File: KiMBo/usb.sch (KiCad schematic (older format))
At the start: 19 parts, among them U1 OSD3358, U10 TPD4S012, U7 TPS2051B, U8 TPD4S012, U9 74LVC2G241

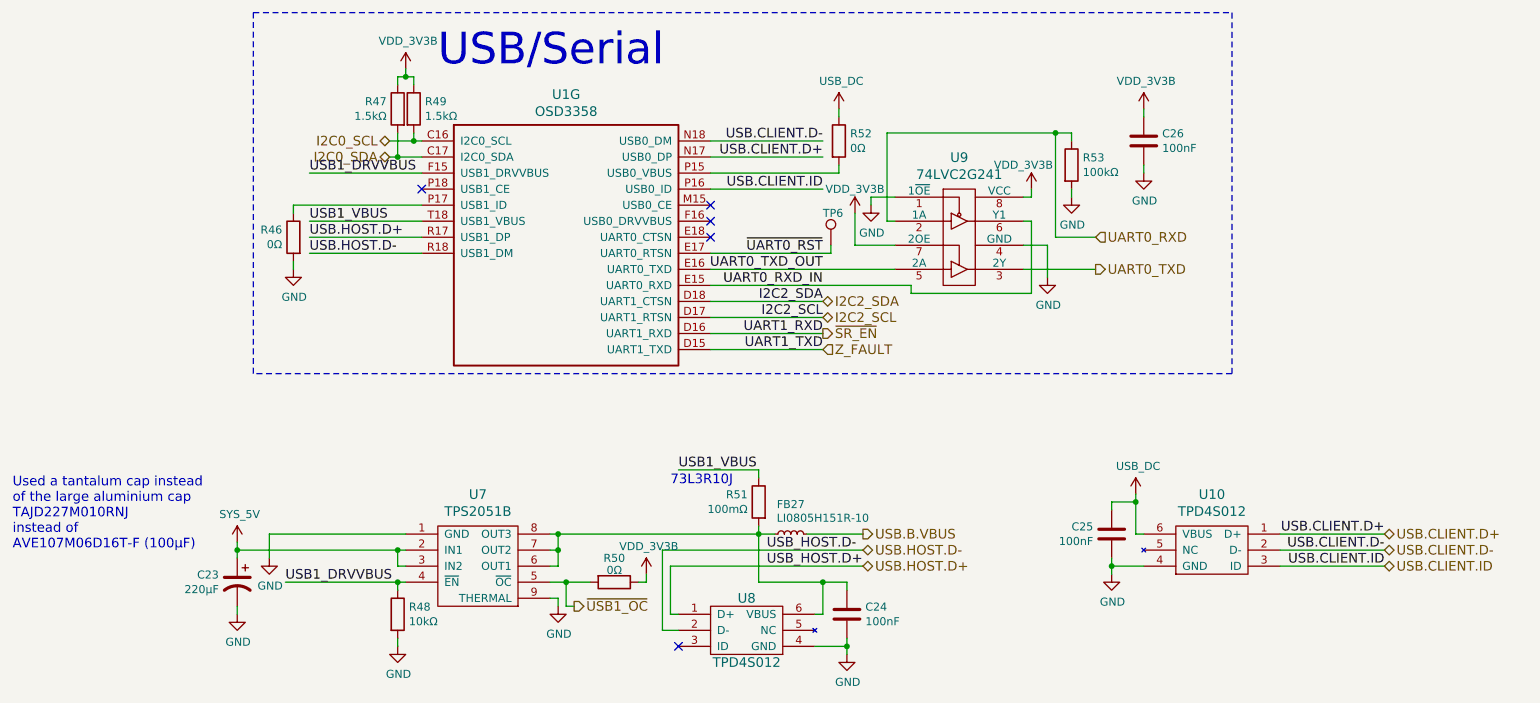
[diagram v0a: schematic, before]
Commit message: Begin layout
Arrange all connectors to get a feel for the area.
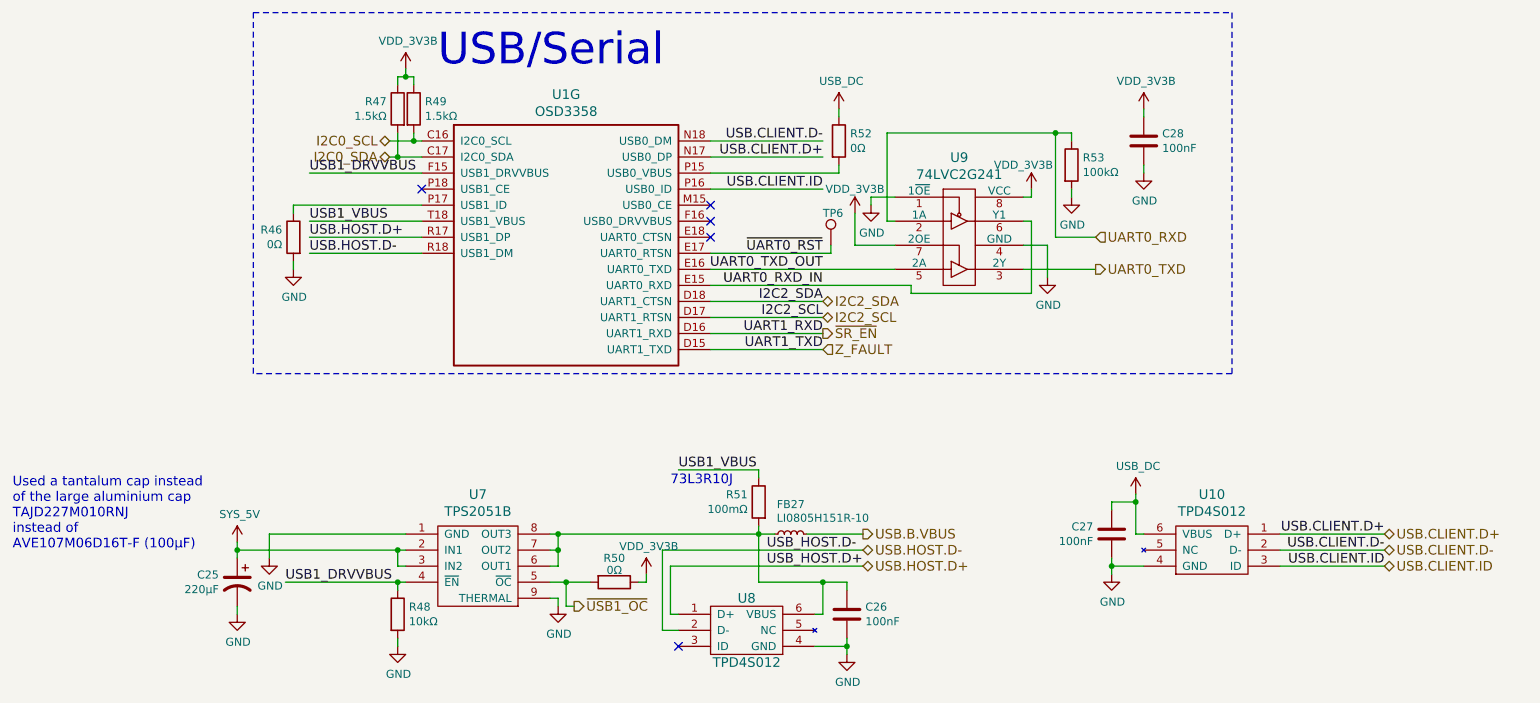
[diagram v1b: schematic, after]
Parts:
- renumbered C23 to C25, C24 to C26, C25 to C27, C26 to C28
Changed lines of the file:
@@
 $EndComp
 $Comp
-L GND #PWR0102
+L GND #PWR0105
 U 1 1 584F5078
 P 7550 2500
-F 0 "#PWR0102" H 7550 2250 50  0001 C CNN
+F 0 "#PWR0105" H 7550 2250 50  0001 C CNN
 F 1 "GND" H 7555 2327 50  0000 C CNN
 F 2 "" H 7550 2500 50  0000 C CNN
@@
 $EndComp
 $Comp
-L GND #PWR0103
+L GND #PWR0106
 U 1 1 584F508C
 P 6450 2050
-F 0 "#PWR0103" H 6450 1800 50  0001 C CNN
+F 0 "#PWR0106" H 6450 1800 50  0001 C CNN
 F 1 "GND" H 6455 1877 50  0000 C CNN
 F 2 "" H 6450 2050 50  0000 C CNN
@@
 UART0_TXD_OUT
 $Comp
-L GND #PWR0104
+L GND #PWR0107
 U 1 1 584F509A
 P 7700 2000
-F 0 "#PWR0104" H 7700 1750 50  0001 C CNN
+F 0 "#PWR0107" H 7700 1750 50  0001 C CNN
 F 1 "GND" H 7705 1827 50  0000 C CNN
 F 2 "" H 7700 2000 50  0000 C CNN
@@
 $EndComp
 $Comp
-L C C26
+L C C28
 U 1 1 584F50A3
 P 8150 1650
-F 0 "C26" H 8265 1696 50  0000 L CNN
+F 0 "C28" H 8265 1696 50  0000 L CNN
 F 1 "100nF" H 8265 1605 50  0000 L CNN
 F 2 "Capacitors_SMD:C_0603" H 8150 1650 50  0001 C CNN
@@
 $EndComp
 $Comp
-L GND #PWR0105
+L GND #PWR0108
 U 1 1 584F50AA
 P 8150 1850
-F 0 "#PWR0105" H 8150 1600 50  0001 C CNN
+F 0 "#PWR0108" H 8150 1600 50  0001 C CNN
 F 1 "GND" H 8155 1677 50  0000 C CNN
 F 2 "" H 8150 1850 50  0000 C CNN
@@
 $EndComp
 $Comp
-L GND #PWR0106
+L GND #PWR0109
 U 1 1 584F50D8
 P 2850 2450
-F 0 "#PWR0106" H 2850 2200 50  0001 C CNN
+F 0 "#PWR0109" H 2850 2200 50  0001 C CNN
 F 1 "GND" H 2855 2277 50  0000 C CNN
 F 2 "" H 2850 2450 50  0000 C CNN
@@
 $EndComp
 $Comp
-L C C24
+L C C26
 U 1 1 58524285
 P 6300 4600
-F 0 "C24" H 6415 4646 50  0000 L CNN
+F 0 "C26" H 6415 4646 50  0000 L CNN
 F 1 "100nF" H 6415 4555 50  0000 L CNN
 F 2 "Capacitors_SMD:C_0603" H 6300 4600 50  0001 C CNN
@@
 $EndComp
 $Comp
-L GND #PWR0107
+L GND #PWR0110
 U 1 1 585243B8
 P 6300 4850
-F 0 "#PWR0107" H 6300 4600 50  0001 C CNN
+F 0 "#PWR0110" H 6300 4600 50  0001 C CNN
 F 1 "GND" H 6305 4677 50  0000 C CNN
 F 2 "" H 6300 4850 50  0000 C CNN
@@
 $EndComp
 $Comp
-L GND #PWR0108
+L GND #PWR0111
 U 1 1 58528602
 P 4500 4550
-F 0 "#PWR0108" H 4500 4300 50  0001 C CNN
+F 0 "#PWR0111" H 4500 4300 50  0001 C CNN
 F 1 "GND" H 4505 4377 50  0000 C CNN
 F 2 "" H 4500 4550 50  0000 C CNN
@@
 $EndComp
 $Comp
-L GND #PWR0109
+L GND #PWR0112
 U 1 1 5852A6BE
 P 2500 4600
-F 0 "#PWR0109" H 2500 4350 50  0001 C CNN
+F 0 "#PWR0112" H 2500 4350 50  0001 C CNN
 F 1 "GND" H 2505 4427 50  0000 C CNN
 F 2 "" H 2500 4600 50  0000 C CNN
@@
 $EndComp
 $Comp
-L GND #PWR0110
+L GND #PWR0113
 U 1 1 5852A82F
 P 2700 4250
-F 0 "#PWR0110" H 2700 4000 50  0001 C CNN
+F 0 "#PWR0113" H 2700 4000 50  0001 C CNN
 F 1 "GND" H 2705 4077 50  0000 C CNN
 F 2 "" H 2700 4250 50  0000 C CNN
@@
 $EndComp
 $Comp
-L GND #PWR0111
+L GND #PWR0114
 U 1 1 5852B68C
 P 3500 4800
-F 0 "#PWR0111" H 3500 4550 50  0001 C CNN
+F 0 "#PWR0114" H 3500 4550 50  0001 C CNN
 F 1 "GND" H 3505 4627 50  0000 C CNN
 F 2 "" H 3500 4800 50  0000 C CNN
@@
 $EndComp
 $Comp
-L C C25
+L C C27
 U 1 1 5852C2E6
 P 7950 4100
-F 0 "C25" H 8065 4146 50  0000 L CNN
+F 0 "C27" H 8065 4146 50  0000 L CNN
 F 1 "100nF" H 8065 4055 50  0000 L CNN
 F 2 "Capacitors_SMD:C_0603" H 7950 4100 50  0001 C CNN
@@
 I2C2_SDA
 $Comp
-L USB_DC #PWR0112
+L USB_DC #PWR0115
 U 1 1 59F94F9A
 P 8100 3850
-F 0 "#PWR0112" H 8100 3700 50  0001 C CNN
+F 0 "#PWR0115" H 8100 3700 50  0001 C CNN
 F 1 "USB_DC" H 8115 4023 50  0000 C CNN
 F 2 "" H 8100 3850 50  0000 C CNN
@@
 $EndComp
 $Comp
-L SYS_5V #PWR0113
+L SYS_5V #PWR0116
 U 1 1 59F970D0
 P 2500 4150
-F 0 "#PWR0113" H 2500 4000 50  0001 C CNN
+F 0 "#PWR0116" H 2500 4000 50  0001 C CNN
 F 1 "SYS_5V" H 2515 4323 50  0000 C CNN
 F 2 "" H 2500 4150 50  0000 C CNN
@@
 $EndComp
 $Comp
-L VDD_3V3B #PWR0114
+L VDD_3V3B #PWR0117
 U 1 1 59FBF8B1
 P 6350 2100
-F 0 "#PWR0114" H 6350 1950 50  0001 C CNN
+F 0 "#PWR0117" H 6350 1950 50  0001 C CNN
 F 1 "VDD_3V3B" H 6350 2250 50  0000 C CNN
 F 2 "" H 6350 2100 50  0000 C CNN
@@
 $EndComp
 $Comp
-L VDD_3V3B #PWR0115
+L VDD_3V3B #PWR0118
 U 1 1 59FBF8FC
 P 7450 1950
-F 0 "#PWR0115" H 7450 1800 50  0001 C CNN
+F 0 "#PWR0118" H 7450 1800 50  0001 C CNN
 F 1 "VDD_3V3B" H 7400 2100 50  0000 C CNN
 F 2 "" H 7450 1950 50  0000 C CNN
@@
 $EndComp
 $Comp
-L VDD_3V3B #PWR0116
+L VDD_3V3B #PWR0119
 U 1 1 59FC0162
 P 8150 1450
-F 0 "#PWR0116" H 8150 1300 50  0001 C CNN
+F 0 "#PWR0119" H 8150 1300 50  0001 C CNN
 F 1 "VDD_3V3B" H 8165 1623 50  0000 C CNN
 F 2 "" H 8150 1450 50  0000 C CNN
@@
 $EndComp
 $Comp
-L USB_DC #PWR0117
+L USB_DC #PWR0120
 U 1 1 59FEDDB0
 P 6250 1450
-F 0 "#PWR0117" H 6250 1300 50  0001 C CNN
+F 0 "#PWR0120" H 6250 1300 50  0001 C CNN
 F 1 "USB_DC" H 6265 1623 50  0000 C CNN
 F 2 "" H 6250 1450 50  0000 C CNN
@@
 $EndComp
 $Comp
-L VDD_3V3B #PWR0118
+L VDD_3V3B #PWR0121
 U 1 1 5A01DA26
 P 3550 1200
-F 0 "#PWR0118" H 3550 1050 50  0001 C CNN
+F 0 "#PWR0121" H 3550 1050 50  0001 C CNN
 F 1 "VDD_3V3B" H 3565 1373 50  0000 C CNN
 F 2 "" H 3550 1200 50  0000 C CNN
@@
 Used a tantalum cap instead\nof the large aluminium cap\nTAJD227M010RNJ\ninstead of\nAVE107M06D16T-F (100μF)
 $Comp
-L VDD_3V3B #PWR0119
+L VDD_3V3B #PWR0122
 U 1 1 5AF563FC
 P 5050 4350
-F 0 "#PWR0119" H 5050 4200 50  0001 C CNN
+F 0 "#PWR0122" H 5050 4200 50  0001 C CNN
 F 1 "VDD_3V3B" H 5065 4523 50  0000 C CNN
 F 2 "" H 5050 4350 50  0000 C CNN
@@
 $EndComp
 $Comp
-L GND #PWR0120
+L GND #PWR0123
 U 1 1 5BC77EEA
 P 7950 4350
-F 0 "#PWR0120" H 7950 4100 50  0001 C CNN
+F 0 "#PWR0123" H 7950 4100 50  0001 C CNN
 F 1 "GND" H 7955 4177 50  0000 C CNN
 F 2 "" H 7950 4350 50  0000 C CNN
@@
 73L3R10J
 $Comp
-L CP1 C23
+L CP1 C25
 U 1 1 58EB0DF2
 P 2500 4400
-F 0 "C23" H 2615 4446 50  0000 L CNN
+F 0 "C25" H 2615 4446 50  0000 L CNN
 F 1 "220μF" H 2615 4355 50  0000 L CNN
 F 2 "Capacitors_Tantalum_SMD:TantalC_SizeD_EIA-7343_Reflow" H 2500 4400 50  0001 C CNN

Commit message: Remove HDMI from the schematic
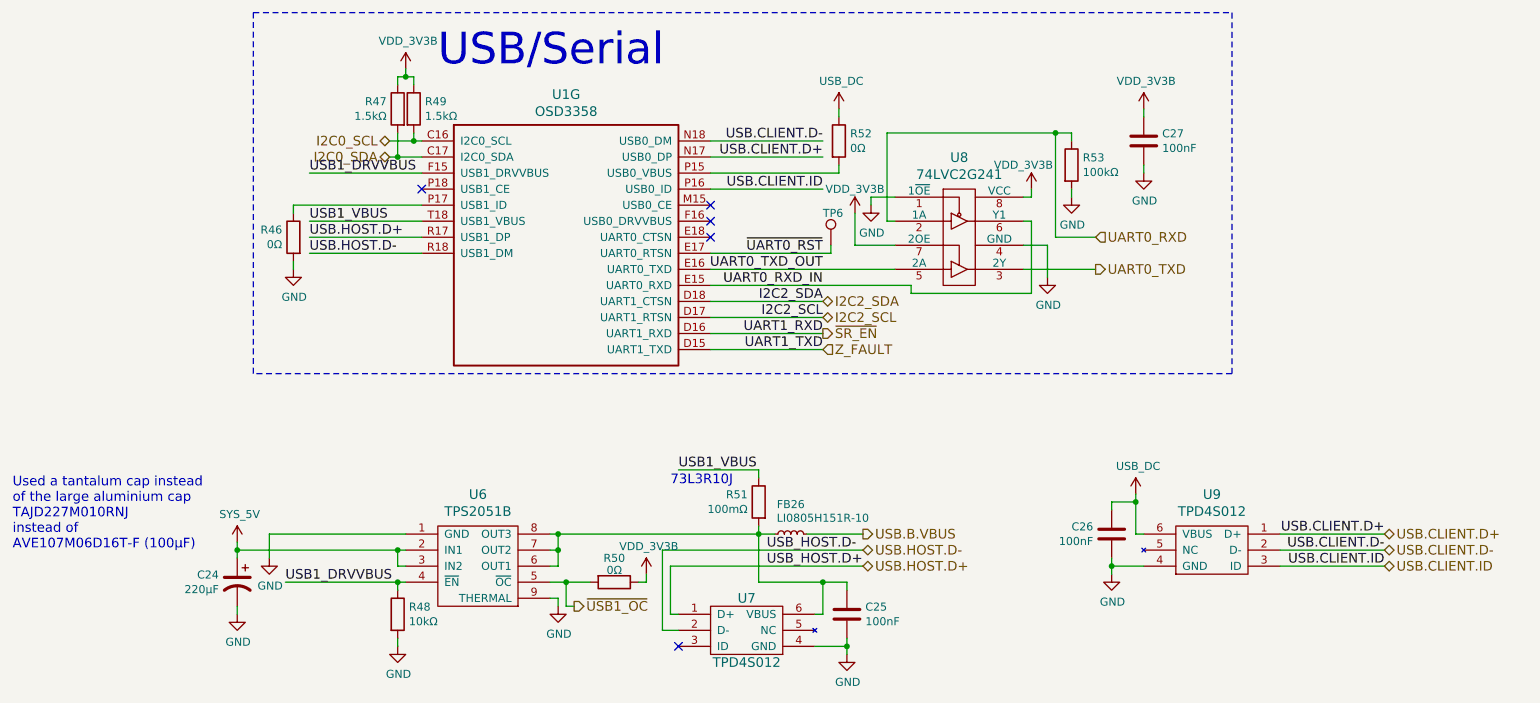
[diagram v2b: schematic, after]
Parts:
- renumbered C25 to C24, C26 to C25, C27 to C26, C28 to C27, FB27 to FB26, U7 to U6, U8 to U7, U9 to U8, U10 to U9
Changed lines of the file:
@@
 $Descr A4 11693 8268
 encoding utf-8
-Sheet 7 26
+Sheet 7 25
 Title ""
 Date ""
@@
 $EndComp
 $Comp
-L 74LVC2G241 U9
+L 74LVC2G241 U8
 U 1 1 584F506B
 P 7000 2200
-F 0 "U9" H 7000 2647 60  0000 C CNN
+F 0 "U8" H 7000 2647 60  0000 C CNN
 F 1 "74LVC2G241" H 7000 2541 60  0000 C CNN
 F 2 "KiMBo:DCT-MSOP-8_3x3mm_Pitch0.65mm" H 7050 1950 60  0001 C CNN
@@
 $EndComp
 $Comp
-L GND #PWR0105
+L GND #PWR0100
 U 1 1 584F5078
 P 7550 2500
-F 0 "#PWR0105" H 7550 2250 50  0001 C CNN
+F 0 "#PWR0100" H 7550 2250 50  0001 C CNN
 F 1 "GND" H 7555 2327 50  0000 C CNN
 F 2 "" H 7550 2500 50  0000 C CNN
@@
 $EndComp
 $Comp
-L GND #PWR0106
+L GND #PWR0101
 U 1 1 584F508C
 P 6450 2050
-F 0 "#PWR0106" H 6450 1800 50  0001 C CNN
+F 0 "#PWR0101" H 6450 1800 50  0001 C CNN
 F 1 "GND" H 6455 1877 50  0000 C CNN
 F 2 "" H 6450 2050 50  0000 C CNN
@@
 UART0_TXD_OUT
 $Comp
-L GND #PWR0107
+L GND #PWR0102
 U 1 1 584F509A
 P 7700 2000
-F 0 "#PWR0107" H 7700 1750 50  0001 C CNN
+F 0 "#PWR0102" H 7700 1750 50  0001 C CNN
 F 1 "GND" H 7705 1827 50  0000 C CNN
 F 2 "" H 7700 2000 50  0000 C CNN
@@
 $EndComp
 $Comp
-L C C28
+L C C27
 U 1 1 584F50A3
 P 8150 1650
-F 0 "C28" H 8265 1696 50  0000 L CNN
+F 0 "C27" H 8265 1696 50  0000 L CNN
 F 1 "100nF" H 8265 1605 50  0000 L CNN
 F 2 "Capacitors_SMD:C_0603" H 8150 1650 50  0001 C CNN
@@
 $EndComp
 $Comp
-L GND #PWR0108
+L GND #PWR0103
 U 1 1 584F50AA
 P 8150 1850
-F 0 "#PWR0108" H 8150 1600 50  0001 C CNN
+F 0 "#PWR0103" H 8150 1600 50  0001 C CNN
 F 1 "GND" H 8155 1677 50  0000 C CNN
 F 2 "" H 8150 1850 50  0000 C CNN
@@
 $EndComp
 $Comp
-L GND #PWR0109
+L GND #PWR0104
 U 1 1 584F50D8
 P 2850 2450
-F 0 "#PWR0109" H 2850 2200 50  0001 C CNN
+F 0 "#PWR0104" H 2850 2200 50  0001 C CNN
 F 1 "GND" H 2855 2277 50  0000 C CNN
 F 2 "" H 2850 2450 50  0000 C CNN
@@
 USB_HOST.D+
 $Comp
-L TPD4S012 U8
+L TPD4S012 U7
 U 1 1 58523D44
 P 5650 4700
-F 0 "U8" H 5675 4900 60  0000 C CNN
+F 0 "U7" H 5675 4900 60  0000 C CNN
 F 1 "TPD4S012" H 5675 4500 60  0000 C CNN
 F 2 "KiMBo:DRY-DFN-6-1EP_2x2mm_Pitch0.5mm" H 5650 4700 60  0001 C CNN
@@
 $EndComp
 $Comp
-L C C26
+L C C25
 U 1 1 58524285
 P 6300 4600
-F 0 "C26" H 6415 4646 50  0000 L CNN
+F 0 "C25" H 6415 4646 50  0000 L CNN
 F 1 "100nF" H 6415 4555 50  0000 L CNN
 F 2 "Capacitors_SMD:C_0603" H 6300 4600 50  0001 C CNN
@@
 $EndComp
 $Comp
-L GND #PWR0110
+L GND #PWR0105
 U 1 1 585243B8
 P 6300 4850
-F 0 "#PWR0110" H 6300 4600 50  0001 C CNN
+F 0 "#PWR0105" H 6300 4600 50  0001 C CNN
 F 1 "GND" H 6305 4677 50  0000 C CNN
 F 2 "" H 6300 4850 50  0000 C CNN
@@
 USB1_VBUS
 $Comp
-L TPS2051B U7
+L TPS2051B U6
 U 1 1 58527077
 P 4000 4250
-F 0 "U7" H 4000 4647 60  0000 C CNN
+F 0 "U6" H 4000 4647 60  0000 C CNN
 F 1 "TPS2051B" H 4000 4541 60  0000 C CNN
 F 2 "KiMBo:DGN-MSOP-8_3x3mm_Pitch0.65mm" H 4000 4200 60  0001 C CNN
@@
 $EndComp
 $Comp
-L GND #PWR0111
+L GND #PWR0106
 U 1 1 58528602
 P 4500 4550
-F 0 "#PWR0111" H 4500 4300 50  0001 C CNN
+F 0 "#PWR0106" H 4500 4300 50  0001 C CNN
 F 1 "GND" H 4505 4377 50  0000 C CNN
 F 2 "" H 4500 4550 50  0000 C CNN
@@
 $EndComp
 $Comp
-L GND #PWR0112
+L GND #PWR0107
 U 1 1 5852A6BE
 P 2500 4600
-F 0 "#PWR0112" H 2500 4350 50  0001 C CNN
+F 0 "#PWR0107" H 2500 4350 50  0001 C CNN
 F 1 "GND" H 2505 4427 50  0000 C CNN
 F 2 "" H 2500 4600 50  0000 C CNN
@@
 $EndComp
 $Comp
-L GND #PWR0113
+L GND #PWR0108
 U 1 1 5852A82F
 P 2700 4250
-F 0 "#PWR0113" H 2700 4000 50  0001 C CNN
+F 0 "#PWR0108" H 2700 4000 50  0001 C CNN
 F 1 "GND" H 2705 4077 50  0000 C CNN
 F 2 "" H 2700 4250 50  0000 C CNN
@@
 $EndComp
 $Comp
-L GND #PWR0114
+L GND #PWR0109
 U 1 1 5852B68C
 P 3500 4800
-F 0 "#PWR0114" H 3500 4550 50  0001 C CNN
+F 0 "#PWR0109" H 3500 4550 50  0001 C CNN
 F 1 "GND" H 3505 4627 50  0000 C CNN
 F 2 "" H 3500 4800 50  0000 C CNN
@@
 $EndComp
 $Comp
-L TPD4S012 U10
+L TPD4S012 U9
 U 1 1 5852BD3E
 P 8600 4200
-F 0 "U10" H 8625 4547 60  0000 C CNN
+F 0 "U9" H 8625 4547 60  0000 C CNN
 F 1 "TPD4S012" H 8625 4441 60  0000 C CNN
 F 2 "KiMBo:DRY-DFN-6-1EP_2x2mm_Pitch0.5mm" H 8600 4200 60  0001 C CNN
@@
 $EndComp
 $Comp
-L C C27
+L C C26
 U 1 1 5852C2E6
 P 7950 4100
-F 0 "C27" H 8065 4146 50  0000 L CNN
+F 0 "C26" H 8065 4146 50  0000 L CNN
 F 1 "100nF" H 8065 4055 50  0000 L CNN
 F 2 "Capacitors_SMD:C_0603" H 7950 4100 50  0001 C CNN
@@
 USB.CLIENT.ID
 $Comp
-L INDUCTOR_Small FB27
+L INDUCTOR_Small FB26
 U 1 1 58E84972
 P 5950 4100
-F 0 "FB27" V 6135 4100 50  0000 C CNN
+F 0 "FB26" V 6135 4100 50  0000 C CNN
 F 1 "LI0805H151R-10" V 6050 3900 50  0000 C CNN
 F 2 "Resistors_SMD:R_0805" H 5950 4100 50  0001 C CNN
@@
 I2C2_SDA
 $Comp
-L USB_DC #PWR0115
+L USB_DC #PWR0110
 U 1 1 59F94F9A
 P 8100 3850
-F 0 "#PWR0115" H 8100 3700 50  0001 C CNN
+F 0 "#PWR0110" H 8100 3700 50  0001 C CNN
 F 1 "USB_DC" H 8115 4023 50  0000 C CNN
 F 2 "" H 8100 3850 50  0000 C CNN
@@
 $EndComp
 $Comp
-L SYS_5V #PWR0116
+L SYS_5V #PWR0111
 U 1 1 59F970D0
 P 2500 4150
-F 0 "#PWR0116" H 2500 4000 50  0001 C CNN
+F 0 "#PWR0111" H 2500 4000 50  0001 C CNN
 F 1 "SYS_5V" H 2515 4323 50  0000 C CNN
 F 2 "" H 2500 4150 50  0000 C CNN
@@
 $EndComp
 $Comp
-L VDD_3V3B #PWR0117
+L VDD_3V3B #PWR0112
 U 1 1 59FBF8B1
 P 6350 2100
-F 0 "#PWR0117" H 6350 1950 50  0001 C CNN
+F 0 "#PWR0112" H 6350 1950 50  0001 C CNN
 F 1 "VDD_3V3B" H 6350 2250 50  0000 C CNN
 F 2 "" H 6350 2100 50  0000 C CNN
@@
 $EndComp
 $Comp
-L VDD_3V3B #PWR0118
+L VDD_3V3B #PWR0113
 U 1 1 59FBF8FC
 P 7450 1950
-F 0 "#PWR0118" H 7450 1800 50  0001 C CNN
+F 0 "#PWR0113" H 7450 1800 50  0001 C CNN
 F 1 "VDD_3V3B" H 7400 2100 50  0000 C CNN
 F 2 "" H 7450 1950 50  0000 C CNN
@@
 $EndComp
 $Comp
-L VDD_3V3B #PWR0119
+L VDD_3V3B #PWR0114
 U 1 1 59FC0162
 P 8150 1450
-F 0 "#PWR0119" H 8150 1300 50  0001 C CNN
+F 0 "#PWR0114" H 8150 1300 50  0001 C CNN
 F 1 "VDD_3V3B" H 8165 1623 50  0000 C CNN
 F 2 "" H 8150 1450 50  0000 C CNN
@@
 $EndComp
 $Comp
-L USB_DC #PWR0120
+L USB_DC #PWR0115
 U 1 1 59FEDDB0
 P 6250 1450
-F 0 "#PWR0120" H 6250 1300 50  0001 C CNN
+F 0 "#PWR0115" H 6250 1300 50  0001 C CNN
 F 1 "USB_DC" H 6265 1623 50  0000 C CNN
 F 2 "" H 6250 1450 50  0000 C CNN
@@
 $EndComp
 $Comp
-L VDD_3V3B #PWR0121
+L VDD_3V3B #PWR0116
 U 1 1 5A01DA26
 P 3550 1200
-F 0 "#PWR0121" H 3550 1050 50  0001 C CNN
+F 0 "#PWR0116" H 3550 1050 50  0001 C CNN
 F 1 "VDD_3V3B" H 3565 1373 50  0000 C CNN
 F 2 "" H 3550 1200 50  0000 C CNN
@@
 Used a tantalum cap instead\nof the large aluminium cap\nTAJD227M010RNJ\ninstead of\nAVE107M06D16T-F (100μF)
 $Comp
-L VDD_3V3B #PWR0122
+L VDD_3V3B #PWR0117
 U 1 1 5AF563FC
 P 5050 4350
-F 0 "#PWR0122" H 5050 4200 50  0001 C CNN
+F 0 "#PWR0117" H 5050 4200 50  0001 C CNN
 F 1 "VDD_3V3B" H 5065 4523 50  0000 C CNN
 F 2 "" H 5050 4350 50  0000 C CNN
@@
 $EndComp
 $Comp
-L GND #PWR0123
+L GND #PWR0118
 U 1 1 5BC77EEA
 P 7950 4350
-F 0 "#PWR0123" H 7950 4100 50  0001 C CNN
+F 0 "#PWR0118" H 7950 4100 50  0001 C CNN
 F 1 "GND" H 7955 4177 50  0000 C CNN
 F 2 "" H 7950 4350 50  0000 C CNN
@@
 73L3R10J
 $Comp
-L CP1 C25
+L CP1 C24
 U 1 1 58EB0DF2
 P 2500 4400
-F 0 "C25" H 2615 4446 50  0000 L CNN
+F 0 "C24" H 2615 4446 50  0000 L CNN
 F 1 "220μF" H 2615 4355 50  0000 L CNN
 F 2 "Capacitors_Tantalum_SMD:TantalC_SizeD_EIA-7343_Reflow" H 2500 4400 50  0001 C CNN

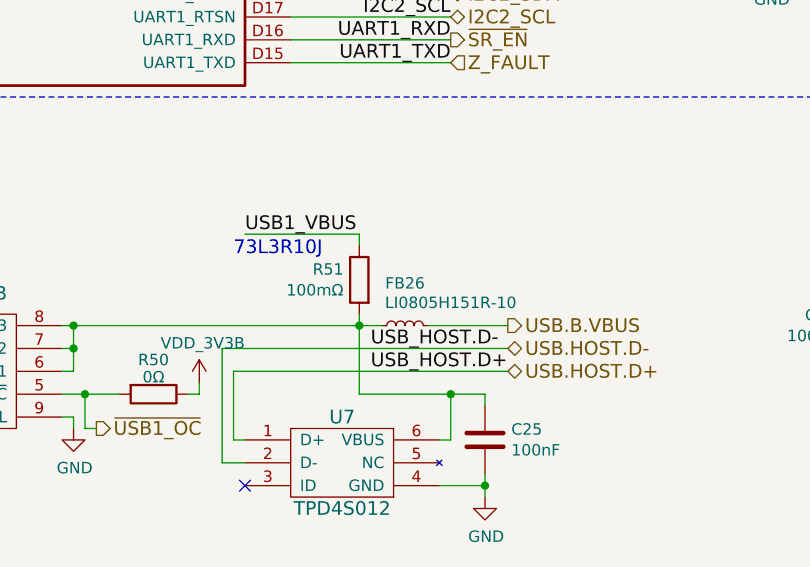
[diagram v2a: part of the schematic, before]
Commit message: Add F1 PTC resettable fuse at the 5V output, begin E's heater circuit layout
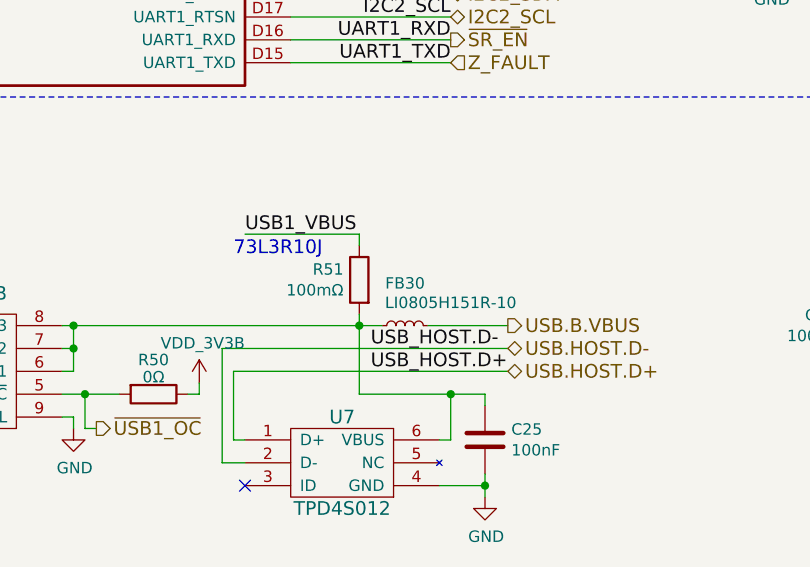
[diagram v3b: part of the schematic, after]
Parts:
- renumbered FB26 to FB30
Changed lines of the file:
@@
 USB.CLIENT.ID
 $Comp
-L INDUCTOR_Small FB26
+L INDUCTOR_Small FB30
 U 1 1 58E84972
 P 5950 4100
-F 0 "FB26" V 6135 4100 50  0000 C CNN
+F 0 "FB30" V 6135 4100 50  0000 C CNN
 F 1 "LI0805H151R-10" V 6050 3900 50  0000 C CNN
 F 2 "Resistors_SMD:R_0805" H 5950 4100 50  0001 C CNN
